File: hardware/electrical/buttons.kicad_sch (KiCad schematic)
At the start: 87 parts

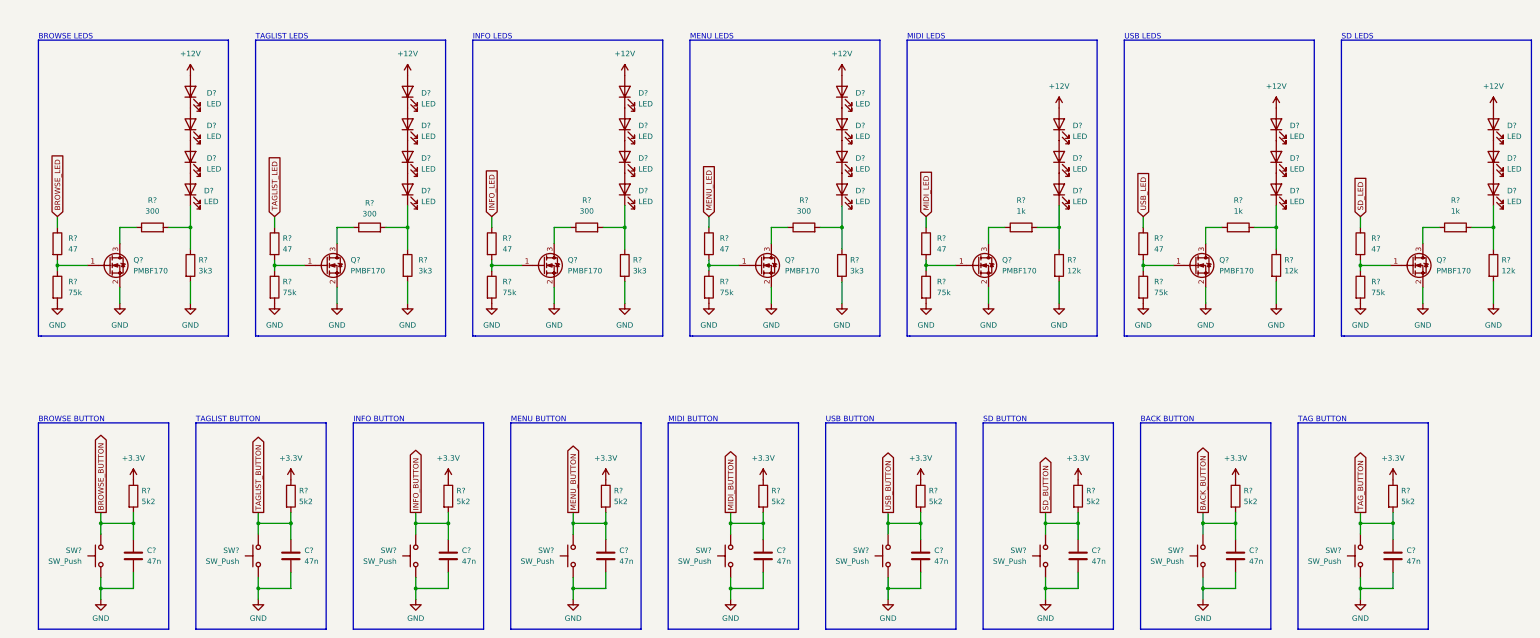
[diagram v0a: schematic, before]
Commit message: Schematic rev. 2 Add second microcontroller to handle encoder, buttons and LEDs Remove external pull-up resistors Simplify LED driver circuits Remove debouncing capacitors Rename SPI connections with standard names Use SPI1 rather than SPI2 Isolate GNDD and GLED
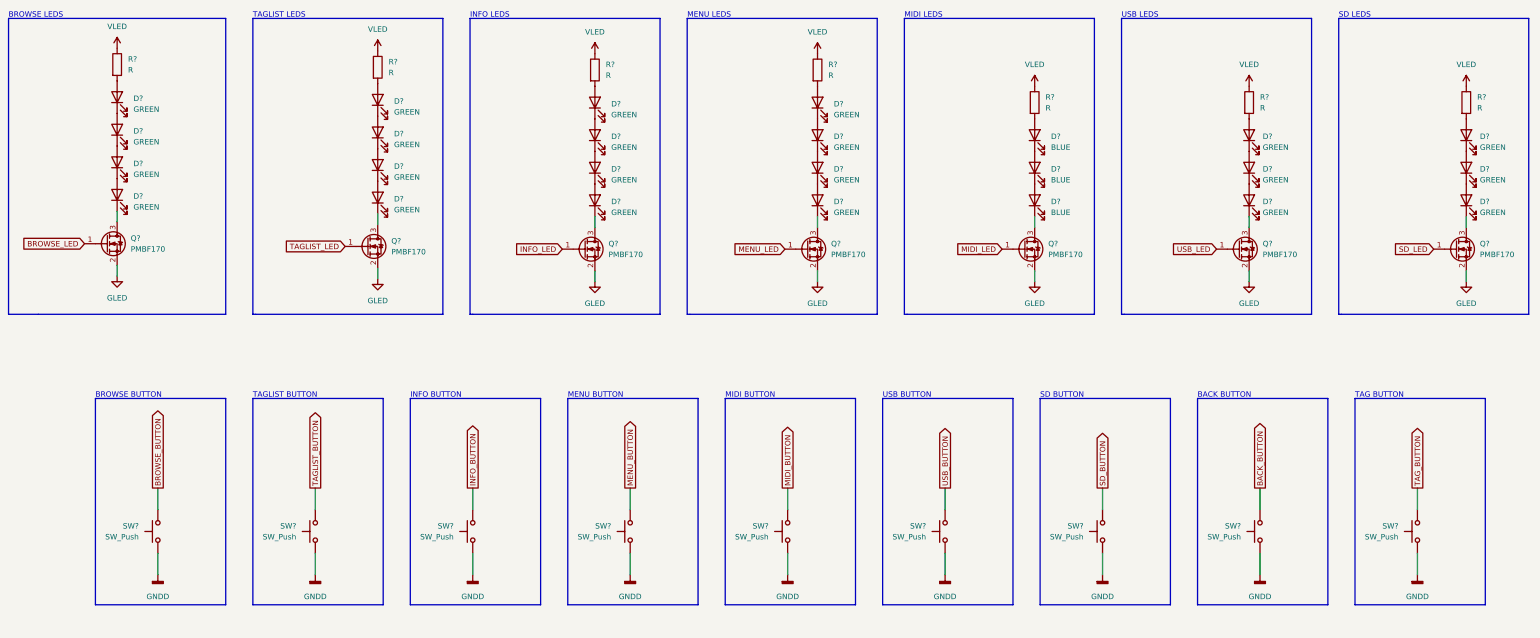
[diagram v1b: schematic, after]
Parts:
- removed C? (x9): 47n, symbol Device:C
- removed D? (x21): LED, symbol Device:LED
- removed Q? (x6): PMBF170, symbol Device:Q_NMOS_GSD
- removed R? (x4): 300, symbol Device:R
- removed R? (x9): 5k2, symbol Device:R
- removed R? (x3): 12k, symbol Device:R
- removed R? (x7): 75k, symbol Device:R
- removed R? (x7): 47, symbol Device:R
- removed R? (x4): 3k3, symbol Device:R
- removed R? (x3): 1k, symbol Device:R
- added D? (x18): GREEN, symbol Device:LED
- added D? (x3): BLUE, symbol Device:LED
- added Q? (x6): PMBF170, symbol Device:Q_NMOS_GSD
- added R? (x7): R, symbol Device:R
- D? (x4): value LED -> GREEN
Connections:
- net BROWSE_LED: now also Q?.1 (G)
- net INFO_LED: now also Q?.1 (G)
- net MENU_LED: now also Q?.1 (G)
- net MIDI_LED: now also Q?.1 (G)
- net SD_LED: now also Q?.1 (G)
- net TAGLIST_LED: now also Q?.1 (G)
- net USB_LED: now also Q?.1 (G)
- net at Q?.3 (D): now also D?.1 (K)
- net +12V: no longer names the net of D?.2 (A)
- net +12V: now also R?.2
- net GND renamed GNDD
- net GNDD: no longer Q?.2 (S)
- new net: D?.1 (K), D?.2 (A) (x15)
- new net: D?.2 (A), R?.2 (x6)
- new net: D?.1 (K), Q?.3 (D) (x6)
- new net GLED: Q?.2 (S), Q?.2 (S), Q?.2 (S), Q?.2 (S), Q?.2 (S), Q?.2 (S), Q?.2 (S)
- new net VLED: R?.1, R?.1, R?.1, R?.1, R?.1, R?.1, R?.1
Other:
- company: (none) -> © ANDREI ANATSKA, FRANK PLOWMAN 2022
- moved on the sheet: D?, Q?, SW?
